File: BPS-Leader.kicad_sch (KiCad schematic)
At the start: 25 parts

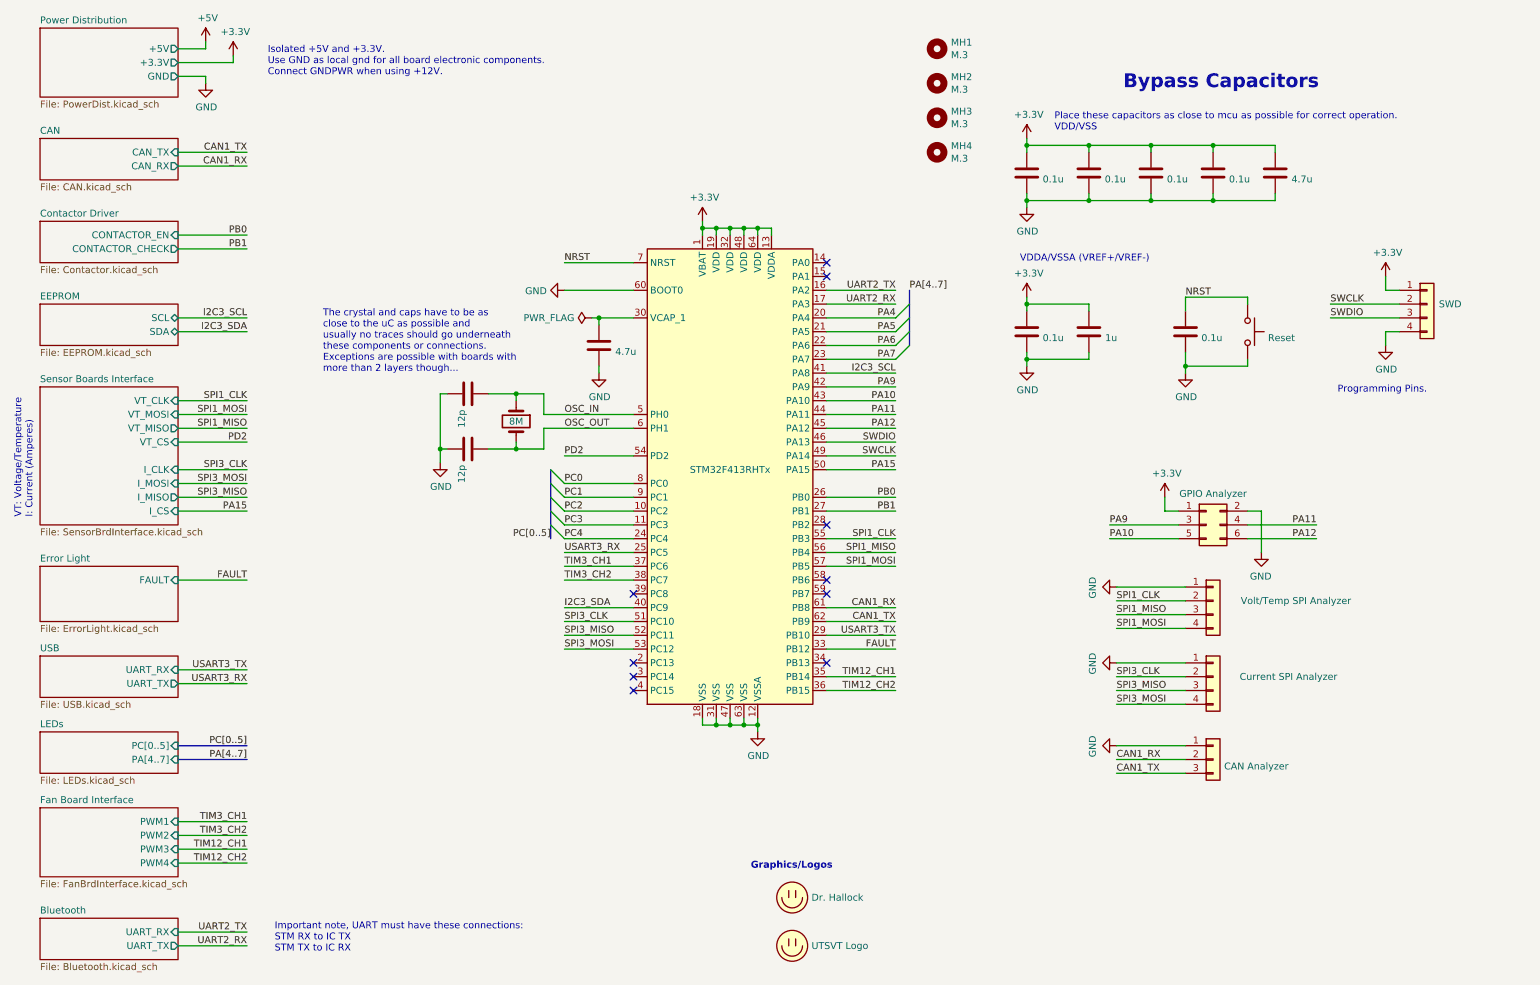
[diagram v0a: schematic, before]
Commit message: Update repo to only use one common library
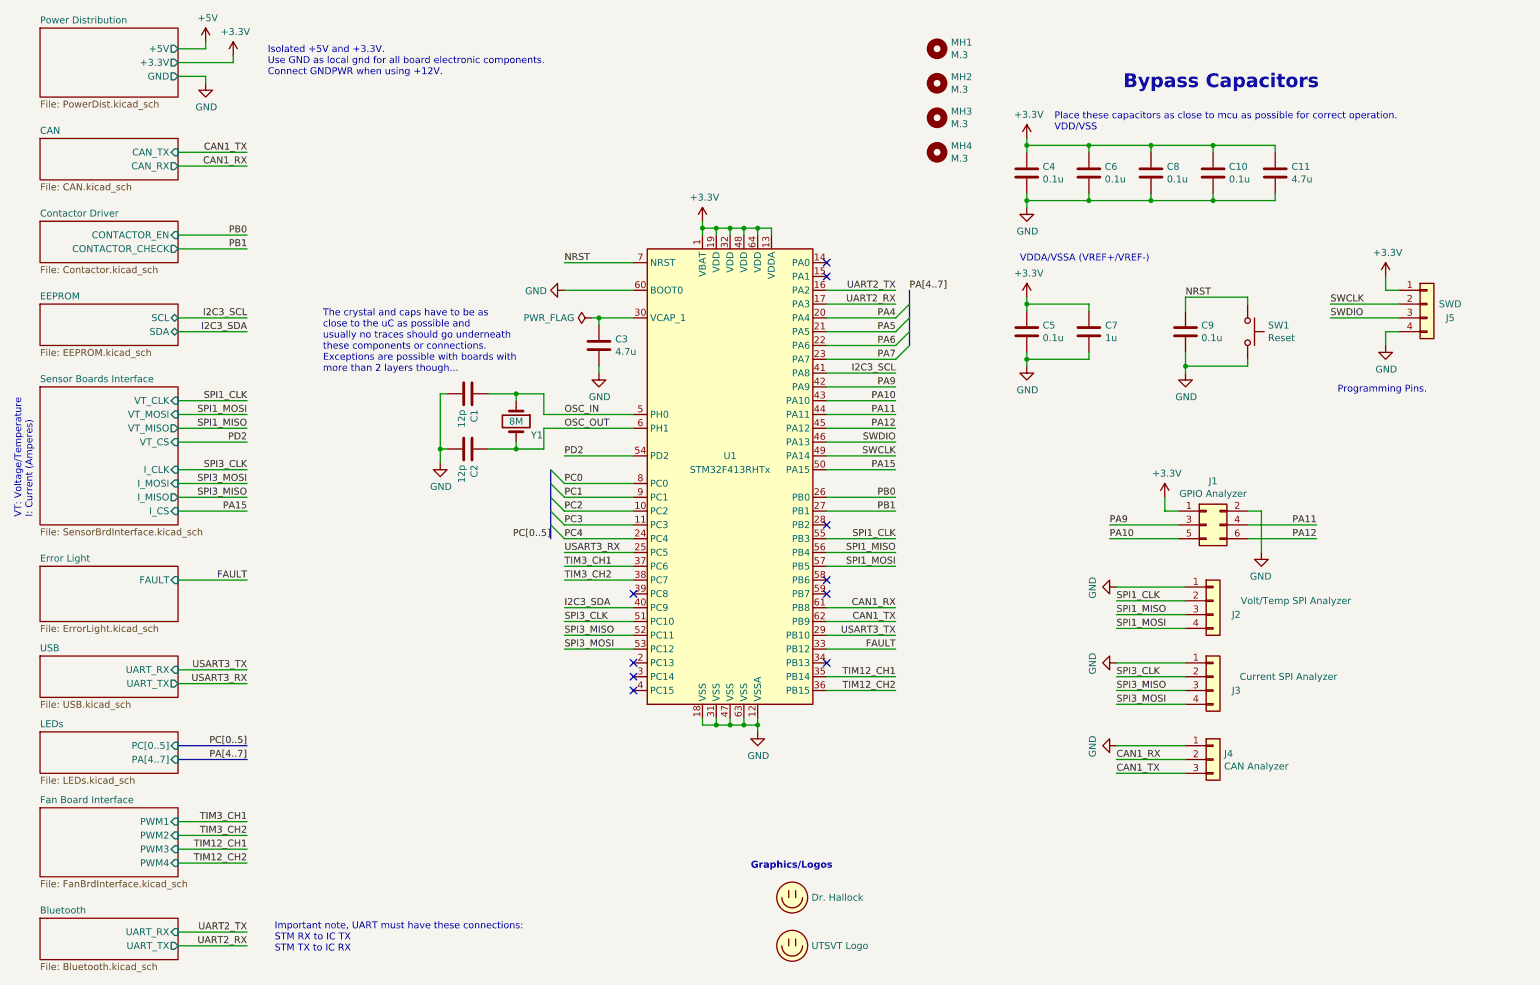
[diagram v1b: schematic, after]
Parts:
- gave numbers to parts that had none: 19
